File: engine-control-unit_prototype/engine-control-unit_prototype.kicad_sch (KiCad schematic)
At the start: 52 parts, among them J1 Micro_SD_Card_Det1, J17 USB_C_Receptacle_USB2.0_man, J3 JTAG, SW1 SW_Push, U2 STM32H747IITx, U9 USBLC6-2SC6, Y1 32.768KHz, Y2 25MHz

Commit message: Added power circuitry without components values
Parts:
- renumbered BT2 to BT1, C3 to C1, C12 to C10, C26 to C11, C27 to C12, C28 to C13, C29 to C14, C30 to C15, C31 to C16, C24 to C17, C25 to C18, C37 to C19, C4 to C2, C43 to C20, C13 to C21, C1 to C22, C2 to C24, C14 to C25, C16 to C26, C18 to C27, C15 to C28, C17 to C29, C5 to C3, C38 to C30, C39 to C31, C34 to C32, C32 to C33, C6 to C4, C7 to C5, C8 to C6, C9 to C7, C10 to C8, C11 to C9, J3 to J1, J17 to J2, J1 to J3, JP2 to JP1, JP3 to JP2, R9 to R1, R1 to R2, R27 to R3, R28 to R4, U9 to U1
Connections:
- net VBAT: no longer names the net of BT1.1 (+), U2.8 (VBAT)
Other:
- moved on the sheet: BT1

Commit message: Modified SD card Fixed INA826 decoupling caps Removed reset button Added Ports connectors (headers for ease of access)
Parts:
- removed C33: 0.1u, symbol Device:C
- removed R3, R4: 5.1k, Resistor_SMD:R_0603_1608Metric_Pad0.98x0.95mm_HandSolder, symbol Device:R
- removed SW1: SW_Push, symbol Switch:SW_Push
- added J10: PORT_B, symbol Connector:Conn_01x16_Socket
- added J11: PORT_C, symbol Connector:Conn_01x16_Socket
- added J12: PORT_D, symbol Connector:Conn_01x16_Socket
- added J13: PORT_A, symbol Connector:Conn_01x16_Socket
- added J14: PORT_G, symbol Connector:Conn_01x16_Socket
- added J15: PORT_F, symbol Connector:Conn_01x16_Socket
- added J16: PORT_E, symbol Connector:Conn_01x16_Socket
- added R3, R4: 5.1k, symbol Device:R_US
- added R37, R40, R41, R42, R45, R46, R51, R52, R53, R54, R55, R56, R57, R58, R59, R60, R61: ?, symbol Device:R_US
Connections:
- net +3V3: now also R55.2, R56.2, R57.2, R58.2, R59.2, R60.2, R61.2
- net CLK_SD1: now also R58.1
- net CMD_SD1: now also R57.1
- net DAT0_SD1: now also R59.1
- net DAT1_SD1: now also R60.1
- net DAT2_SD1: now also R55.1
- net DAT3_SD1: now also R56.1
- net DET_SD1: now also R61.1
- net ECU_Analog/PT1: no longer U2.41 (PA0)
- net ECU_Analog/PT2: no longer U2.42 (PA1)
- net ECU_Communication/FDCAN1_RX: no longer U2.130 (PA11)
- net ECU_Communication/FDCAN1_TX: no longer U2.131 (PA12)
- net ECU_eMMC/eMMC_CLK: now also R53.1
- net ECU_eMMC/eMMC_CMD: now also R54.1
- net ECU_eMMC/eMMC_DAT1: now also R40.1
- net ECU_eMMC/eMMC_DAT2: now also R41.1
- net ECU_eMMC/eMMC_DAT3: now also R42.1
- net ECU_eMMC/eMMC_DAT4: now also R45.1
- net ECU_eMMC/eMMC_DAT5: now also R46.1
- net ECU_eMMC/eMMC_DAT6: now also R51.1
- net ECU_eMMC/eMMC_DAT7: now also R52.1
- net ECU_eMMC/eMMC_DTA0: now also R37.1
- net GND: now also R3.1, R4.1
- net at J2.B5 (CC2): now also R4.2
- net at BZ1.1: no longer names the net of BZ1.1
- net at J2.A5 (CC1): now also R3.2
- net at U2.1 (PE2): now also J16.3 (Pin_3)
- net at U2.10 (PC14): now also J11.15 (Pin_15)
- net at U2.11 (PC15): now also J11.16 (Pin_16)
- net at U2.110 (PG2): now also J14.3 (Pin_3)
- net at U2.111 (PG3): now also J14.4 (Pin_4)
- net at U2.114 (PG4): now also J14.5 (Pin_5)
- net at U2.115 (PG5): now also J14.6 (Pin_6)
- net at U2.116 (PG6): now also J14.7 (Pin_7)
- net at U2.117 (PG7): now also J14.8 (Pin_8)
- net at U2.118 (PG8): now also J14.9 (Pin_9)
- net at U2.122 (PC6): now also J11.7 (Pin_7)
- net at U2.123 (PC7): now also J11.8 (Pin_8)
- net at U2.124 (PC8): now also J11.9 (Pin_9)
- net at U2.125 (PC9): now also J11.10 (Pin_10)
- net at U2.127 (PA8): now also J13.9 (Pin_9)
- net at U2.128 (PA9): now also J13.10 (Pin_10)
- net at U2.129 (PA10): now also J13.11 (Pin_11)
- net at U2.132 (PA13): now also J13.14 (Pin_14)
- net at U2.138 (PA14): now also J13.15 (Pin_15)
- net at U2.139 (PA15): now also J13.16 (Pin_16)
- net at U2.140 (PC10): now also J11.11 (Pin_11)
- net at U2.141 (PC11): now also J11.12 (Pin_12)
- net at U2.142 (PC12): now also J11.13 (Pin_13)
- net at U2.143 (PD0): now also J12.1 (Pin_1)
- net at U2.144 (PD1): now also J12.2 (Pin_2)
- net at U2.145 (PD2): now also J12.3 (Pin_3)
- net at U2.146 (PD3): now also J12.4 (Pin_4)
- net at U2.147 (PD4): now also J12.5 (Pin_5)
- net at U2.148 (PD5): now also J12.6 (Pin_6)
- net at U2.149 (PD6): now also J12.7 (Pin_7)
- net at U2.150 (PD7): now also J12.8 (Pin_8)
- net at U2.153 (PG9): now also J14.10 (Pin_10)
- net at U2.154 (PG10): now also J14.11 (Pin_11)
- net at U2.155 (PG11): now also J14.12 (Pin_12)
- net at U2.156 (PG12): now also J14.13 (Pin_13)
- net at U2.157 (PG13): now also J14.14 (Pin_14)
- net at U2.158 (PG14): now also J14.15 (Pin_15)
- net at U2.161 (PG15): now also J14.16 (Pin_16)
- net at U2.162 (PB3): now also J10.4 (Pin_4)
- net at U2.163 (PB4): now also J10.5 (Pin_5)
- net at U2.164 (PB5): now also J10.6 (Pin_6)
- net at U2.165 (PB6): now also J10.7 (Pin_7)
- net at U2.166 (PB7): now also J10.8 (Pin_8)
- net at U2.168 (PB8): now also J10.9 (Pin_9)
- net at U2.169 (PB9): now also J10.10 (Pin_10)
- net at U2.170 (PE0): now also J16.1 (Pin_1)
- net at U2.171 (PE1): now also J16.2 (Pin_2)
- net at U2.18 (PF0): now also J15.1 (Pin_1)
- net at U2.19 (PF1): now also J15.2 (Pin_2)
- net at U2.2 (PE3): now also J16.4 (Pin_4)
- net at U2.20 (PF2): now also J15.3 (Pin_3)
- net at U2.21 (PF3): now also J15.4 (Pin_4)
- net at U2.22 (PF4): now also J15.5 (Pin_5)
- net at U2.23 (PF5): now also J15.6 (Pin_6)
- net at U2.26 (PF6): now also J15.7 (Pin_7)
- net at U2.27 (PF7): now also J15.8 (Pin_8)
- net at U2.28 (PF8): now also J15.9 (Pin_9)
- net at U2.29 (PF9): now also J15.10 (Pin_10)
- net at U2.3 (PE4): now also J16.5 (Pin_5)
- net at U2.30 (PF10): now also J15.11 (Pin_11)
- net at U2.34 (PC0): now also J11.1 (Pin_1)
- net at U2.35 (PC1): now also J11.2 (Pin_2)
- net at U2.36 (PC2_C): now also J11.3 (Pin_3)
- net at U2.37 (PC3_C): now also J11.4 (Pin_4)
- net at U2.4 (PE5): now also J16.6 (Pin_6)
- net at U2.43 (PA2): now also J13.3 (Pin_3)
- net at U2.46 (PA3): now also J13.4 (Pin_4)
- net at U2.49 (PA4): now also J13.5 (Pin_5)
- net at U2.5 (PE6): now also J16.7 (Pin_7)
- net at U2.50 (PA5): now also J13.6 (Pin_6)
- net at U2.51 (PA6): now also J13.7 (Pin_7)
- net at U2.52 (PA7): now also J13.8 (Pin_8)
- net at U2.53 (PC4): now also J11.5 (Pin_5)
- net at U2.54 (PC5): now also J11.6 (Pin_6)
- net at U2.55 (PB0): now also J10.1 (Pin_1)
- net at U2.56 (PB1): now also J10.2 (Pin_2)
- net at U2.57 (PB2): now also J10.3 (Pin_3)
- net at U2.58 (PF11): now also J15.12 (Pin_12)
- net at U2.59 (PF12): now also J15.13 (Pin_13)
- net at U2.60 (PF13): now also J15.14 (Pin_14)
- net at U2.61 (PF14): now also J15.15 (Pin_15)
- net at U2.62 (PF15): now also J15.16 (Pin_16)
- net at U2.63 (PG0): now also J14.1 (Pin_1)
- net at U2.66 (PG1): now also J14.2 (Pin_2)
- net at U2.67 (PE7): now also J16.8 (Pin_8)
- net at U2.68 (PE8): now also J16.9 (Pin_9)
- net at U2.69 (PE9): now also J16.10 (Pin_10)
- net at U2.72 (PE10): now also J16.11 (Pin_11)
- net at U2.73 (PE11): now also J16.12 (Pin_12)
- net at U2.74 (PE12): now also J16.13 (Pin_13)
- net at U2.75 (PE13): now also J16.14 (Pin_14)
- net at U2.76 (PE14): now also J16.15 (Pin_15)
- net at U2.77 (PE15): now also J16.16 (Pin_16)
- net at U2.78 (PB10): now also J10.11 (Pin_11)
- net at U2.79 (PB11): now also J10.12 (Pin_12)
- net at U2.85 (PB12): now also J10.13 (Pin_13)
- net at U2.86 (PB13): now also J10.14 (Pin_14)
- net at U2.87 (PB14): now also J10.15 (Pin_15)
- net at U2.88 (PB15): now also J10.16 (Pin_16)
- net at U2.89 (PD8): now also J12.9 (Pin_9)
- net at U2.9 (PC13): now also J11.14 (Pin_14)
- net at U2.90 (PD9): now also J12.10 (Pin_10)
- net at U2.91 (PD10): now also J12.11 (Pin_11)
- net at U2.94 (PD11): now also J12.12 (Pin_12)
- net at U2.95 (PD12): now also J12.13 (Pin_13)
- net at U2.96 (PD13): now also J12.14 (Pin_14)
- net at U2.97 (PD14): now also J12.15 (Pin_15)
- net at U2.98 (PD15): now also J12.16 (Pin_16)
- new net: J13.1 (Pin_1), U2.41 (PA0)
- new net: J13.12 (Pin_12), U2.130 (PA11)
- new net: J13.13 (Pin_13), U2.131 (PA12)
- new net: J13.2 (Pin_2), U2.42 (PA1)
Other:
- note added: "Checker temp"
- note removed: "On s'était pourtant entendu sur ce microchip"
- note removed: "STM à changer. trop de pins dans pas gros"
- note removed: "Switch probablement a retirer"

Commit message: Removed bloat libraries Changed symbols for Sirius custom library Changed layout for one page
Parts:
- removed R37, R40, R41, R42, R45, R46, R51, R52, R53, R54: ?, symbol Device:R_US
- removed U2: STM32H747IITx, Package_QFP:LQFP-176_24x24mm_P0.5mm, symbol MCU_ST_STM32H7:STM32H747IITx
- added C33, C35, C47: 0.1u, symbol Device:C
- added C34: 10u, symbol Device:C
- added C36, C37, C39, C42, C43, C45: ?, symbol Device:C
- added C38, C44: C, symbol Device:C
- added C46: 100nF, symbol Device:C
- added C48: Creg, symbol Device:C
- added C49: CVCCQ1, symbol Device:C
- added C50: CVCCQ2, symbol Device:C
- added C51: CVCC1, symbol Device:C
- added C52: CVCC2, symbol Device:C
- added C67: 4.7u ESR < 100m, symbol Device:C
- added C68, C69: 2.2u ESR < 100m, symbol Device:C
- added C70, C71: 4.7u, symbol Device:C
- added C72: 220p, symbol Device:C
- added C73, C74: 10u ESR < 20m, symbol Device:C
- added J4, J6: PT1, symbol Connector:Screw_Terminal_01x04
- added J5, J7: VREF, symbol Connector:Conn_01x01_Pin
- added J8: FDCAN, symbol Connector:DE9_Pins_MountingHoles
- added JP10, JP11, JP12, JP6, JP7: SMPS, symbol Jumper:SolderJumper_2_Open
- added JP3, JP4: PIN/GND, symbol Jumper:Jumper_3_Bridged12
- added JP5, JP8, JP9: LDO, symbol Jumper:SolderJumper_2_Open
- added L3: FBMJ1608HM180NTR, symbol Device:L_Ferrite
- added L4: 2.2u, symbol Device:L
- added R10, R6: ?, symbol Device:R_US
- added R11, R12, R5, R7, R8, R9: 0, symbol Device:R_US
- added R13, R14, R15, R16, R17, R18, R19, R20, R21, R24: R_US, symbol Device:R_US
- added U2: ~, Package_BGA:LFBGA-153_11.5x13mm_Layout14x14_P0.5mm, symbol FSU_LIB:ASFC32G31T3-51BIN
- added U3, U4: INA826, UserFootprints:SOP65P490X110-8N, symbol INA826:INA826AIDGKR
- added U5: TCAN337G, symbol Interface_CAN_LIN:TCAN337G
- added U7: STM32H747II, Package_QFP:LQFP-176_24x24mm_P0.5mm, symbol FSU_LIB:STM32H747II
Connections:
- net +3V3: now also C46.1, U5.3 (VCC)
- net BOOT0: now also U7.167 (BOOT0)
- net GND: now also C46.2, C47.2, C48.2, C49.2, C50.2, C51.2, C52.2, C68.2, C69.2, J8.0 (PAD), J8.3, J8.6, R13.2, U2.A6 (VSS), U2.C4 (VSSQ), U2.E7 (VSS), U2.G5 (VSS), U2.H10 (VSS), U2.J5 (VSS), U2.K8 (VSS), U2.N2 (VSSQ), U2.N5 (VSSQ), U2.P4 (VSSQ), U2.P6 (VSSQ), U5.2 (GND), U7.100 (VSS), U7.112 (VSS), U7.119 (VSS), U7.12 (VSS), U7.134 (VSS), U7.137 (VSS), U7.151 (VSS), U7.159 (VSS), U7.173 (VSS), U7.24 (VSS), U7.45 (VSS), U7.47 (VSS), U7.6 (VSS), U7.64 (VSS), U7.70 (VSS), U7.81 (VSS), U7.83 (VSS), U7.93 (VSS)
- net GNDA: now also C33.1, C34.1, C35.1, C36.2, C38.1, C39.1, C42.2, C44.1, C45.1, J4.4 (Pin_4), J6.4 (Pin_4), JP3.1 (A), JP4.1 (A), U3.5 (V-), U4.5 (V-)
- net NRST: now also U7.33 (NRST)
- net VCAP: now also JP10.2 (B), JP11.2 (B), JP6.2 (B), JP8.2 (B), JP9.2 (B), U7.133 (VCAP), U7.172 (VCAP), U7.80 (VCAP)
- net VCAPDSI: now also U7.101 (VCAPDSI)
- net VDD33_USB: now also U7.121 (VDD33_USB)
- net VDD55_USB: now also U7.120 (VDD50_USB)
- net VDDA: now also C33.2, C34.2, C35.2, J4.1 (Pin_1), J6.1 (Pin_1), U3.8 (V+), U4.8 (V+), U7.40 (VDDA)
- net VDDLDO: now also JP5.2 (B), JP7.1 (A), U7.175 (VDDLDO)
- net VDDSMPS: now also C67.1, L3.2, U7.16 (VDDSMPS)
- net VDD_MCU: now also JP5.1 (A), L3.1, U7.113 (VDD), U7.126 (VDD), U7.13 (VDD), U7.136 (VDD), U7.152 (VDD), U7.160 (VDD), U7.176 (VDD), U7.25 (VDD), U7.44 (VDD), U7.48 (VDD), U7.65 (VDD), U7.7 (VDD), U7.71 (VDD), U7.84 (VDD), U7.92 (VDD), U7.99 (VDD)
- net VREF+: now also U7.39 (VREF+)
- net VSSA: now also U7.38 (VSSA)
- net VSSDSI: now also U7.105 (VSSDSI), U7.109 (VSSDSI)
- net VSSSMPS: now also C67.2, C70.2, C71.2, C72.2, C73.2, C74.2, U7.14 (VSSSMPS)
- net at J15.1 (Pin_1): now also U7.18 (PF0)
- net at J15.10 (Pin_10): now also U7.29 (PF9)
- net at J15.11 (Pin_11): now also U7.30 (PF10)
- net at J15.12 (Pin_12): now also U7.58 (PF11)
- net at J15.13 (Pin_13): now also U7.59 (PF12)
- net at J15.14 (Pin_14): now also U7.60 (PF13)
- net at J15.15 (Pin_15): now also U7.61 (PF14)
- net at J15.16 (Pin_16): now also U7.62 (PF15)
- net at J15.2 (Pin_2): now also U7.19 (PF1)
- net at J15.3 (Pin_3): now also U7.20 (PF2)
- net at J15.4 (Pin_4): now also U7.21 (PF3)
- net at J15.5 (Pin_5): now also U7.22 (PF4)
- net at J15.6 (Pin_6): now also U7.23 (PF5)
- net at J15.7 (Pin_7): now also U7.26 (PF6)
- net at J15.8 (Pin_8): now also U7.27 (PF7)
- net at J15.9 (Pin_9): now also U7.28 (PF8)
- net at J16.1 (Pin_1): now also U7.170 (PE0)
- net at J16.10 (Pin_10): now also U7.69 (PE9)
- net at J16.11 (Pin_11): now also U7.72 (PE10)
- net at J16.12 (Pin_12): now also U7.73 (PE11)
- net at J16.13 (Pin_13): now also U7.74 (PE12)
- net at J16.14 (Pin_14): now also U7.75 (PE13)
- net at J16.15 (Pin_15): now also U7.76 (PE14)
- net at J16.16 (Pin_16): now also U7.77 (PE15)
- net at J16.2 (Pin_2): now also U7.171 (PE1)
- net at J16.3 (Pin_3): now also U7.1 (PE2)
- net at J16.4 (Pin_4): now also U7.2 (PE3)
- net at J16.5 (Pin_5): now also U7.3 (PE4)
- net at J16.6 (Pin_6): now also U7.4 (PE5)
- net at J16.7 (Pin_7): now also U7.5 (PE6)
- net at J16.8 (Pin_8): now also U7.67 (PE7)
- net at J16.9 (Pin_9): now also U7.68 (PE8)
- net at J10.1 (Pin_1): now also U7.55 (PB0)
- net at J10.10 (Pin_10): now also U7.169 (PB9)
- net at J10.11 (Pin_11): now also U7.78 (PB10)
- net at J10.12 (Pin_12): now also U7.79 (PB11)
- net at J10.13 (Pin_13): now also U7.85 (PB12)
- net at J10.14 (Pin_14): now also U7.86 (PB13)
- net at J10.15 (Pin_15): now also U7.87 (PB14)
- net at J10.16 (Pin_16): now also U7.88 (PB15)
- net at J10.2 (Pin_2): now also U7.56 (PB1)
- net at J10.3 (Pin_3): now also U7.57 (PB2)
- net at J10.4 (Pin_4): now also U7.162 (PB3)
- net at J10.5 (Pin_5): now also U7.163 (PB4)
- net at J10.6 (Pin_6): now also U7.164 (PB5)
- net at J10.7 (Pin_7): now also U7.165 (PB6)
- net at J10.8 (Pin_8): now also U7.166 (PB7)
- net at J10.9 (Pin_9): now also U7.168 (PB8)
- net at J13.1 (Pin_1): now also U7.41 (PA0)
- net at J13.10 (Pin_10): now also U7.128 (PA9)
- net at J13.11 (Pin_11): now also U7.129 (PA10)
- net at J13.12 (Pin_12): now also U7.130 (PA11)
- net at J13.13 (Pin_13): now also U7.131 (PA12)
- net at J13.14 (Pin_14): now also U7.132 (PA13)
- net at J13.15 (Pin_15): now also U7.138 (PA14)
- net at J13.16 (Pin_16): now also U7.139 (PA15)
- net at J13.2 (Pin_2): now also U7.42 (PA1)
- net at J13.3 (Pin_3): now also U7.43 (PA2)
- net at J13.4 (Pin_4): now also U7.46 (PA3)
- net at J13.5 (Pin_5): now also U7.49 (PA4)
- net at J13.6 (Pin_6): now also U7.50 (PA5)
- net at J13.7 (Pin_7): now also U7.51 (PA6)
- net at J13.8 (Pin_8): now also U7.52 (PA7)
- net at J13.9 (Pin_9): now also U7.127 (PA8)
- net at J12.1 (Pin_1): now also U7.143 (PD0)
- net at J12.10 (Pin_10): now also U7.90 (PD9)
- net at J12.11 (Pin_11): now also U7.91 (PD10)
- net at J12.12 (Pin_12): now also U7.94 (PD11)
- net at J12.13 (Pin_13): now also U7.95 (PD12)
- net at J12.14 (Pin_14): now also U7.96 (PD13)
- net at J12.15 (Pin_15): now also U7.97 (PD14)
- net at J12.16 (Pin_16): now also U7.98 (PD15)
- net at J12.2 (Pin_2): now also U7.144 (PD1)
- net at J12.3 (Pin_3): now also U7.145 (PD2)
- net at J12.4 (Pin_4): now also U7.146 (PD3)
- net at J12.5 (Pin_5): now also U7.147 (PD4)
- net at J12.6 (Pin_6): now also U7.148 (PD5)
- net at J12.7 (Pin_7): now also U7.149 (PD6)
- net at J12.8 (Pin_8): now also U7.150 (PD7)
- net at J12.9 (Pin_9): now also U7.89 (PD8)
- net at BT1.1 (+): now also U7.8 (VBAT)
- net at J14.1 (Pin_1): now also U7.63 (PG0)
- net at J14.10 (Pin_10): now also U7.153 (PG9)
- net at J14.11 (Pin_11): now also U7.154 (PG10)
- net at J14.12 (Pin_12): now also U7.155 (PG11)
- net at J14.13 (Pin_13): now also U7.156 (PG12)
- net at J14.14 (Pin_14): now also U7.157 (PG13)
- net at J14.15 (Pin_15): now also U7.158 (PG14)
- net at J14.16 (Pin_16): now also U7.161 (PG15)
- net at J14.2 (Pin_2): now also U7.66 (PG1)
- net at J14.3 (Pin_3): now also U7.110 (PG2)
- net at J14.4 (Pin_4): now also U7.111 (PG3)
- net at J14.5 (Pin_5): now also U7.114 (PG4)
- net at J14.6 (Pin_6): now also U7.115 (PG5)
- net at J14.7 (Pin_7): now also U7.116 (PG6)
- net at J14.8 (Pin_8): now also U7.117 (PG7)
- net at J14.9 (Pin_9): now also U7.118 (PG8)
- net at J11.15 (Pin_15): now also U7.10 (PC14)
- net at J11.16 (Pin_16): now also U7.11 (PC15)
- net at J11.7 (Pin_7): now also U7.122 (PC6)
- net at J11.8 (Pin_8): now also U7.123 (PC7)
- net at J11.9 (Pin_9): now also U7.124 (PC8)
- net at J11.10 (Pin_10): now also U7.125 (PC9)
- net at J11.11 (Pin_11): now also U7.140 (PC10)
- net at J11.12 (Pin_12): now also U7.141 (PC11)
- net at J11.13 (Pin_13): now also U7.142 (PC12)
- net at J11.1 (Pin_1): now also U7.34 (PC0)
- net at J11.2 (Pin_2): now also U7.35 (PC1)
- net at J11.3 (Pin_3): now also U7.36 (PC2_C)
- net at J11.4 (Pin_4): now also U7.37 (PC3_C)
- net at J11.5 (Pin_5): now also U7.53 (PC4)
- net at J11.6 (Pin_6): now also U7.54 (PC5)
- net at J11.14 (Pin_14): now also U7.9 (PC13)
- new net: C70.1, JP10.1 (A)
- new net: C71.1, JP11.1 (A)
- new net: C37.1, C39.2, R8.1, U3.4 (+)
- new net: J5.1 (Pin_1), JP3.3 (B)
- new net: R11.2, U4.7 (Vout)
- new net: J7.1 (Pin_1), JP4.3 (B)
- new net: C68.1, JP8.1 (A)
- new net: C43.1, C45.2, R12.1, U4.4 (+)
- new net: J8.2, U5.6 (CANL)
- new net: J8.7, U5.7 (CANH)
- new net: C36.1, C37.2, R5.1, U3.1 (-)
- new net: C42.1, C43.2, R9.1, U4.1 (-)
- new net: R7.2, U3.7 (Vout)
- new net: JP4.2 (C), U4.6 (REF)
- new net: C74.1, JP12.1 (A)
- new net: R10.1, U4.3 (RG)
- new net: R10.2, U4.2 (RG)
- new net: C69.1, JP9.1 (A)
- new net: JP3.2 (C), U3.6 (REF)
- new net: R6.1, U3.3 (RG)
- new net: R6.2, U3.2 (RG)
- new net +IN1: J4.2 (Pin_2), R8.2
- new net +IN2: J6.2 (Pin_2), R12.2
- new net -IN1: J4.3 (Pin_3), R5.2
- new net -IN2: J6.3 (Pin_3), R9.2
- new net PT1: C38.2, R7.1
- new net PT2: C44.2, R11.1
- new net TCAN_RX: U5.1 (TXD)
- new net TCAN_STBY: R13.1, U5.8 (S)
- new net TCAN_TX: U5.4 (RXD)
- new net VDD: C47.1, C48.1, C49.1, C50.1, C51.1, C52.1, R14.1, R15.1, R16.1, R17.1, R18.1, R19.1, R20.1, R21.1, R24.1, U2.C2 (VDDI), U2.C6 (VCCQ), U2.E6 (VCC), U2.F5 (VCC), U2.J10 (VCC), U2.K9 (VCC), U2.M4 (VCCQ), U2.N4 (VCCQ), U2.P3 (VCCQ), U2.P5 (VCCQ)
- new net VFBSMPS: C73.1, JP12.2 (B), JP6.1 (A), JP7.2 (B), L4.2, U7.17 (VFBSMPS)
- new net VLXSMPS: C72.1, L4.1, U7.15 (VLXSMPS)
- new net eMMC_CLK: U2.M6 (CLK)
- new net eMMC_CMD: R24.2, U2.M5 (CMD)
- new net eMMC_DAT0: R14.2, U2.A3 (DAT0)
- new net eMMC_DAT1: R15.2, U2.A4 (DAT1)
- new net eMMC_DAT2: R16.2, U2.A5 (DAT2)
- new net eMMC_DAT3: R17.2, U2.B2 (DAT3)
- new net eMMC_DAT4: R18.2, U2.B3 (DAT4)
- new net eMMC_DAT5: R19.2, U2.B4 (DAT5)
- new net eMMC_DAT6: R20.2, U2.B5 (DAT6)
- new net eMMC_DAT7: R21.2, U2.B6 (DAT7)
- no-connect marks 7 -> 13
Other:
- removed sheet ECU_Analog
- removed sheet ECU_Communication
- removed sheet ECU_SMPS
- removed sheet ECU_eMMC
- note added: "(1)"
- note added: "(1) Jumpers pour choix entre SMPS direct ou SMPS externe avec LDO par SMPS"
- note added: "(1) This resistor is optional if the input voltage stays above [(V-) - 2 V] or if the signal source current drive capability is limited to less than 3.5 mA; see the Input Protection section for more details."
- note added: "(2)"
- note added: "(2) Bead utilisé dans eval board"
- note added: "(2) The output of the INA826 is referred to the output reference (REF) terminal, which is normally grounded. This connection must be low-impedance to maintain good common-mode rejection. Although 5 Ω or less of stray resistance can be tolerated when maintaining specified CMRR, small stray resistances of tens of ohms in series with the REF pin can cause noticeable degradation in CMRR."
- note added: "(3)"
- note added: "(3) Choix des condensateurs pour SMPS [p.103, p.110 | stm32h757ai.pdf]"
- note added: "(3) Pour filtrage si nécéssaire"
- note added: "(4)"
- note added: "(4) Datasheet dit 4.7uF, mais eval board met 10uF"
- note added: "(4) Proche des pins d'alim"
- note added: "(5) Gain = 1 + $9.4k/Rg"
- note added: "ALIMENTATION/DECOUPLING"
- note added: "ASFC32G31T3-51BIN"
- note added: "ATTENTION 3.3v pas branché a VDD"
- note added: "C0G CAPS pour vibrations"
- note added: "Datasheet STM32H747"
- note added: "Impédance match data = 50±5 ohm"
- note added: "PRESSURE TRANSDUCERS"
- note added: "Placer proche L1"
- note added: "SMPS"
- note added: "Schematic Eval board STM32H7X7"
- note added: "eMMC"
- note removed: "Display Serial Interface"
- moved on the sheet: BT1, BZ1, C1, C10, C11, C12, C13, C14, C15, C16, C17, C18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

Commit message: Removed some more bloated libraries
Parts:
- added C40, C54, C56: 0.1u, symbol Device:C
- added C41: 10u, symbol Device:C
- added C53, C55, C57: C, symbol Device:C
- added C58: CIN, symbol Device:C_Polarized_US
- added C59: COUT, symbol Device:C_Polarized_US
- added C60: CdV/dT, symbol Device:C
- added D3: TVS SMBJ, symbol Device:D_Schottky
- added IC1: TPS259573DSGR, SON50P200X200X80-9N, symbol TPS259573DSGR:TPS259573DSGR
- added J17: 2S_18650, symbol Connector:Screw_Terminal_01x02
- added R22, R23, R25, R26, R27, R28, R30, R31, R37, R40: R_US, symbol Device:R_US
- added R29, R41, R42: 10m, symbol Device:R_US
- added TP10: IN2-, symbol Connector:TestPoint
- added TP11: IN3+, symbol Connector:TestPoint
- added TP12: IN3-, symbol Connector:TestPoint
- added TP7: IN1+, symbol Connector:TestPoint
- added TP8: IN1-, symbol Connector:TestPoint
- added TP9: IN2+, symbol Connector:TestPoint
- added U13, U6, U8: INA219AxD, Package_SO:SOIC-8_3.9x4.9mm_P1.27mm, symbol Sensor_Energy:INA219AxD
- added U14: LT3042xMSE, Package_SO:MSOP-10-1EP_3x3mm_P0.5mm_EP1.68x1.88mm, symbol Regulator_Linear:LT3042xMSE
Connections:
- net +3V3: now also C40.2, C41.2, C54.2, C56.2, R26.2, R31.2, R42.2, TP10.1, U13.1 (A1), U13.5 (VS), U6.5 (VS), U8.2 (A0), U8.5 (VS)
- net GND: now also C40.1, C41.1, C54.1, C56.1, C58.2, C59.2, C60.2, D3.2 (A), IC1.8 (GND_1), IC1.9 (GND_2), J17.2 (Pin_2), R37.2, R40.2, U13.2 (A0), U13.6 (GND), U6.1 (A1), U6.2 (A0), U6.6 (GND), U8.1 (A1), U8.6 (GND)
- new net: IC1.7 (ILM), R40.1
- new net: IC1.2 (~{EN}/OVLO), R30.2, R37.1
- new net: C55.1, R26.1, U8.7 (IN-)
- new net: C53.1, R23.1, U6.7 (IN-)
- new net: C53.2, R22.1, U6.8 (IN+)
- new net: C55.2, R25.1, U8.8 (IN+)
- new net: U14.1 (IN), U14.2 (IN)
- new net: U14.11 (GND), U14.8 (GND)
- new net: C57.1, R28.1, U13.7 (IN-)
- new net: C57.2, R27.1, U13.8 (IN+)
- new net: C60.1, IC1.1 (DVDT)
- new net +10V: R28.2, R41.2, TP12.1
- new net +BATT1: C58.1, D3.1 (K), IC1.3 (IN_1), IC1.4 (IN_2), J17.1 (Pin_1), R30.1
- new net FLT: IC1.6 (~{FLT}), R31.1
- new net Psense1_IN+: C59.1, IC1.5 (OUT), R22.2, R29.1, TP7.1
- new net Psense2_IN+: R25.2, R42.1, TP9.1
- new net Psense3_IN+: R27.2, R41.1, TP11.1
- new net SCL: U13.4 (SCL), U6.4 (SCL), U8.4 (SCL)
- new net SDA: U13.3 (SDA), U6.3 (SDA), U8.3 (SDA)
- new net VBAT_SAFE: R23.2, R29.2, TP8.1
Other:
- removed sheet ECU_Power
- note added: "10V REGULATION"
- note added: "3V3 REGULATION"
- note added: "Calcul des compos"
- note added: "INPUT PROTECTION"
- note added: "Jumper pour adresses ?"
- note added: "PSENSE"

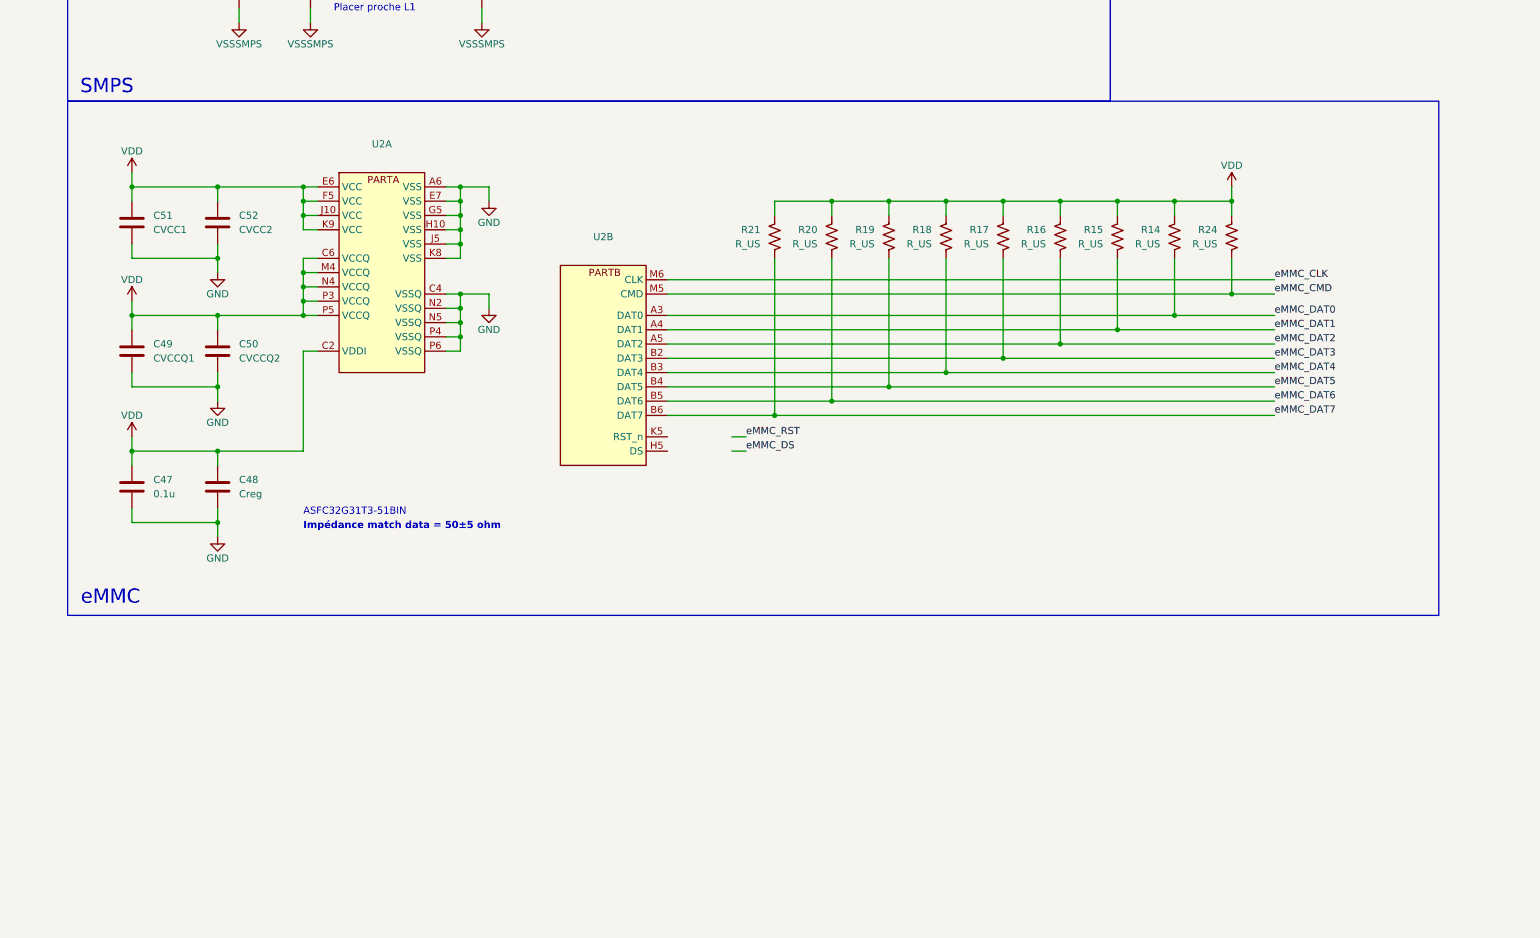
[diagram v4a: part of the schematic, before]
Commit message: Modif eMMC, devrait etre good (A review avec geg).
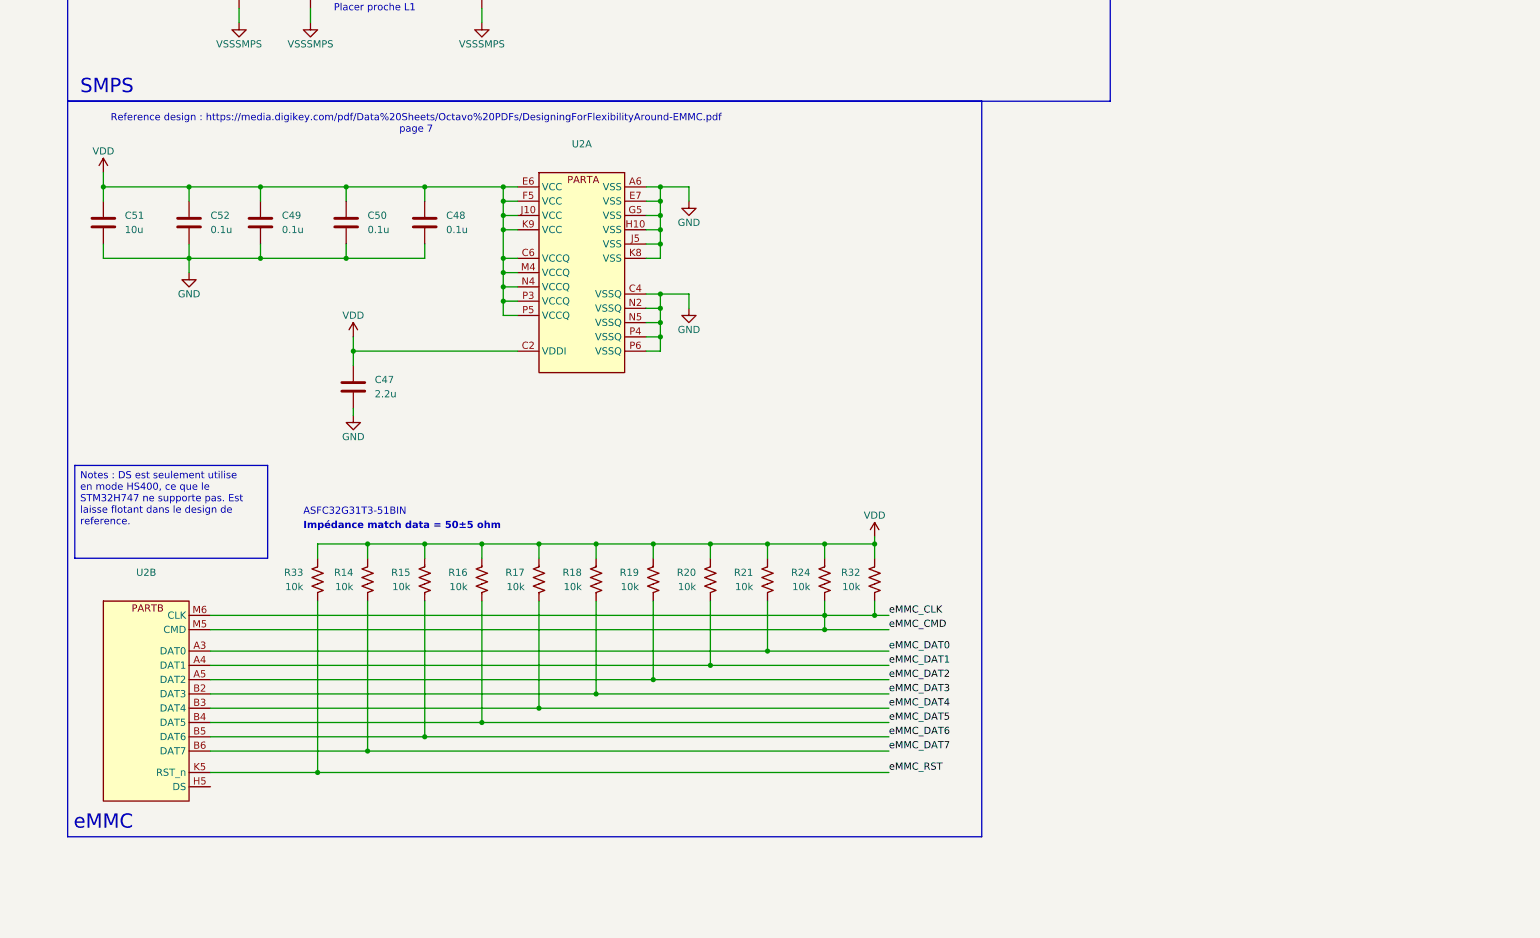
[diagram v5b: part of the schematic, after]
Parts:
- added R32, R33: 10k, symbol Device:R_US
- C47: value 0.1u -> 2.2u
- C48: value Creg -> 0.1u
- C49: value CVCCQ1 -> 0.1u
- C50: value CVCCQ2 -> 0.1u
- C51: value CVCC1 -> 10u
- C52: value CVCC2 -> 0.1u
- R14, R15, R16, R17, R18, R19, R20, R21, R24: value R_US -> 10k
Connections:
- net eMMC_CMD is gone; now on net eMMC_CLK: R24.2, U2.M5 (CMD)
- net VDD: now also R32.1, R33.1
- net eMMC_CLK: now also R32.2
- net eMMC_DAT0: now also R21.2; no longer R14.2
- net eMMC_DAT1: now also R20.2; no longer R15.2
- net eMMC_DAT2: now also R19.2; no longer R16.2
- net eMMC_DAT3: now also R18.2; no longer R17.2
- net eMMC_DAT4: now also R17.2; no longer R18.2
- net eMMC_DAT5: now also R16.2; no longer R19.2
- net eMMC_DAT6: now also R15.2; no longer R20.2
- net eMMC_DAT7: now also R14.2; no longer R21.2
- net eMMC_RST: now also U2.K5 (RST_n), R33.2
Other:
- note added: "Reference design : https://media.digikey.com/pdf/Data%20Sheets/Octavo%20PDFs/DesigningForFlexibilityAround-EMMC.pdf page 7"
- moved on the sheet: C47, C49, C50, C51, C52, U2A, U2B
